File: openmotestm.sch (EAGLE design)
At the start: 46 parts, among them X1 PHB_1MM27_2X05_SNS

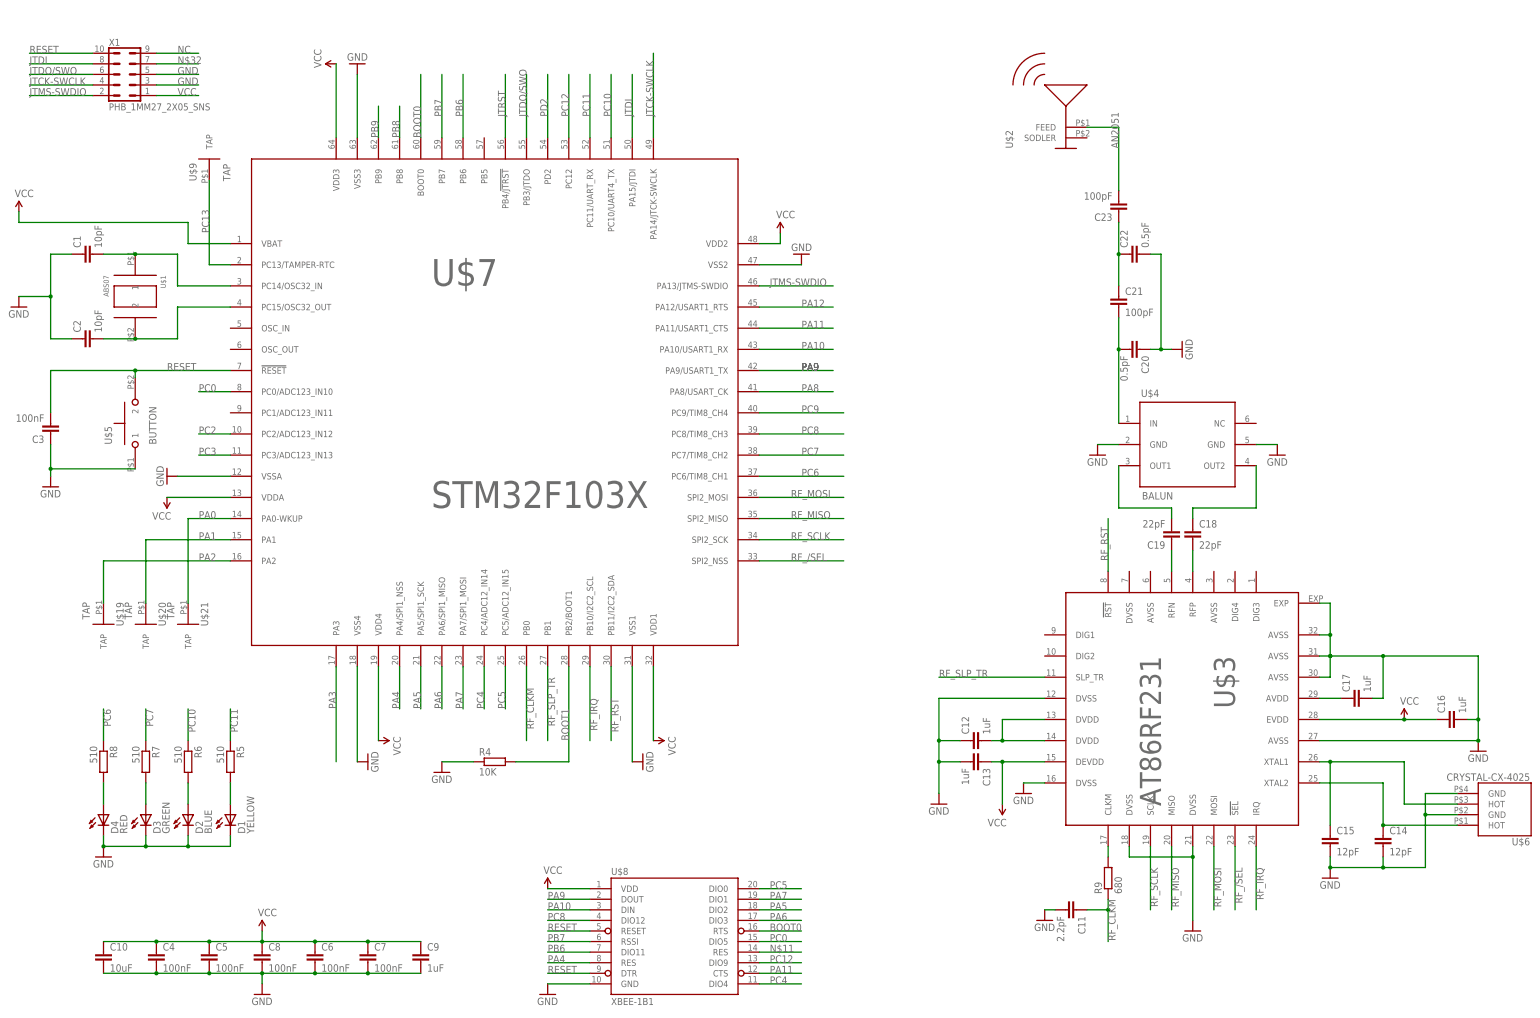
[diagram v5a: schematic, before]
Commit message: Fix the package of chips.
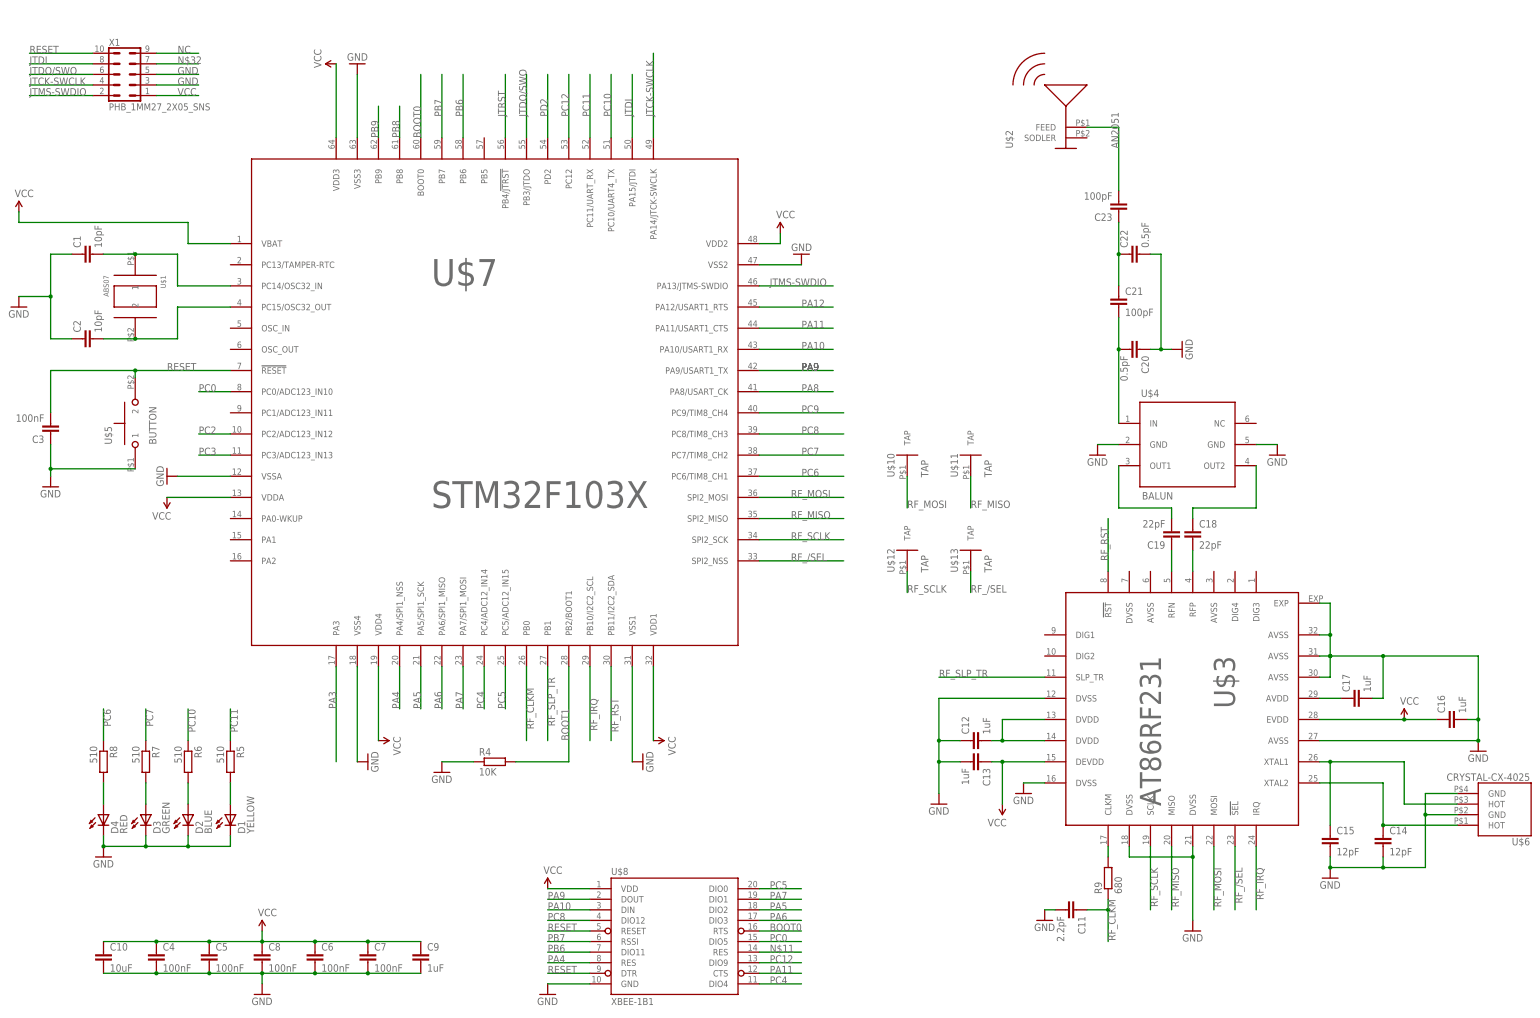
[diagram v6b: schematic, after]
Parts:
- removed U$19, U$20, U$21, U$9: TAP, openmotestm:TAP
- added U$10, U$11, U$12, U$13: TAP, openmotestm:TAP
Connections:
- removed net PA0: U$21.TAP, U$7.PA0-WKUP
- removed net PA1: U$20.TAP, U$7.PA1
- removed net PA2: U$19.TAP, U$7.PA2
- removed net PC13: U$7.PC13/TAMPER-RTC, U$9.TAP
- net RF_/SEL: now also U$13.TAP
- net RF_MISO: now also U$11.TAP
- net RF_MOSI: now also U$10.TAP
- net RF_SCLK: now also U$12.TAP
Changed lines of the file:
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@@
 <layer number="19" name="Unrouted" color="6" fill="1" visible="no" active="no"/>
 <layer number="20" name="Dimension" color="15" fill="1" visible="no" active="no"/>
-<layer number="21" name="tPlace" color="7" fill="1" visible="no" active="no"/>
-<layer number="22" name="bPlace" color="7" fill="1" visible="no" active="no"/>
+<layer number="21" name="tPlace" color="14" fill="1" visible="no" active="no"/>
+<layer number="22" name="bPlace" color="6" fill="1" visible="no" active="no"/>
 <layer number="23" name="tOrigins" color="15" fill="1" visible="no" active="no"/>
 <layer number="24" name="bOrigins" color="15" fill="1" visible="no" active="no"/>
-<layer number="25" name="tNames" color="7" fill="1" visible="no" active="no"/>
+<layer number="25" name="tNames" color="15" fill="1" visible="no" active="no"/>
 <layer number="26" name="bNames" color="7" fill="1" visible="no" active="no"/>
 <layer number="27" name="tValues" color="7" fill="1" visible="no" active="no"/>
@@
 <part name="GND20" library="SparkFun-Aesthetics" deviceset="GND" device=""/>
 <part name="SUPPLY5" library="SparkFun-Aesthetics" deviceset="VCC" device=""/>
-<part name="U$9" library="openmotestm" deviceset="TAP" device=""/>
-<part name="U$19" library="openmotestm" deviceset="TAP" device=""/>
-<part name="U$20" library="openmotestm" deviceset="TAP" device=""/>
-<part name="U$21" library="openmotestm" deviceset="TAP" device=""/>
 <part name="U$6" library="openmotestm" deviceset="CRYSTAL-CX-4025" device=""/>
 <part name="C12" library="rcl" deviceset="C-EU" device="C0603" value="1uF"/>
@@
 <part name="C10" library="rcl" deviceset="C-EU" device="C0603" value="10uF"/>
 <part name="X1" library="_hhn_con_pinhead_box_1mm27" deviceset="PHB_1MM27_2X05_*" device="SNS"/>
+<part name="U$10" library="openmotestm" deviceset="TAP" device=""/>
+<part name="U$11" library="openmotestm" deviceset="TAP" device=""/>
+<part name="U$12" library="openmotestm" deviceset="TAP" device=""/>
+<part name="U$13" library="openmotestm" deviceset="TAP" device=""/>
 </parts>
 <sheets>
@@
 <instance part="GND20" gate="1" x="-134.62" y="25.4" rot="R270"/>
 <instance part="SUPPLY5" gate="G$1" x="-134.62" y="20.32" rot="R180"/>
-<instance part="U$9" gate="G$1" x="-124.46" y="99.06"/>
-<instance part="U$19" gate="G$1" x="-149.86" y="-7.62" rot="R180"/>
-<instance part="U$20" gate="G$1" x="-139.7" y="-7.62" rot="R180"/>
-<instance part="U$21" gate="G$1" x="-129.54" y="-7.62" rot="R180"/>
 <instance part="U$6" gate="G$1" x="185.42" y="-53.34" rot="R180"/>
 <instance part="C12" gate="G$1" x="58.42" y="-38.1" rot="R90"/>
@@
 <instance part="C10" gate="G$1" x="-149.86" y="-88.9"/>
 <instance part="X1" gate="G$1" x="-144.78" y="121.92"/>
+<instance part="U$10" gate="G$1" x="43.18" y="27.94"/>
+<instance part="U$11" gate="G$1" x="58.42" y="27.94"/>
+<instance part="U$12" gate="G$1" x="43.18" y="5.08"/>
+<instance part="U$13" gate="G$1" x="58.42" y="5.08"/>
 </instances>
 <busses>
@@
 <label x="15.24" y="20.32" size="1.778" layer="95"/>
 </segment>
+<segment>
+<pinref part="U$10" gate="G$1" pin="TAP"/>
+<wire x1="43.18" y1="25.4" x2="43.18" y2="17.78" width="0.1524" layer="91"/>
+<label x="43.18" y="17.78" size="1.778" layer="95"/>
+</segment>
 </net>
 <net name="RF_MISO" class="0">
@@
 <label x="15.24" y="15.24" size="1.778" layer="95"/>
 </segment>
+<segment>
+<pinref part="U$11" gate="G$1" pin="TAP"/>
+<wire x1="58.42" y1="25.4" x2="58.42" y2="17.78" width="0.1524" layer="91"/>
+<label x="58.42" y="17.78" size="1.778" layer="95"/>
+</segment>
 </net>
 <net name="RF_SCLK" class="0">
@@
 <label x="15.24" y="10.16" size="1.778" layer="95"/>
 </segment>
+<segment>
+<pinref part="U$12" gate="G$1" pin="TAP"/>
+<wire x1="43.18" y1="2.54" x2="43.18" y2="-2.54" width="0.1524" layer="91"/>
+<label x="43.18" y="-2.54" size="1.778" layer="95"/>
+</segment>
 </net>
 <net name="RF_/SEL" class="0">
@@
 <wire x1="121.92" y1="-63.5" x2="121.92" y2="-78.74" width="0.1524" layer="91"/>
 <label x="121.92" y="-68.58" size="1.778" layer="95" rot="R270"/>
+</segment>
+<segment>
+<pinref part="U$13" gate="G$1" pin="TAP"/>
+<wire x1="58.42" y1="2.54" x2="58.42" y2="-2.54" width="0.1524" layer="91"/>
+<label x="58.42" y="-2.54" size="1.778" layer="95"/>
 </segment>
 </net>
@@
 </segment>
 </net>
-<net name="PC13" class="0">
-<segment>
-<pinref part="U$7" gate="G$1" pin="PC13/TAMPER-RTC"/>
-<wire x1="-119.38" y1="76.2" x2="-124.46" y2="76.2" width="0.1524" layer="91"/>
-<label x="-124.46" y="83.82" size="1.778" layer="95" rot="R90"/>
-<wire x1="-124.46" y1="76.2" x2="-124.46" y2="96.52" width="0.1524" layer="91"/>
-<pinref part="U$9" gate="G$1" pin="TAP"/>
-</segment>
-</net>
 <net name="PC10" class="0">
 <segment>
@@
 </segment>
 </net>
-<net name="PA0" class="0">
-<segment>
-<pinref part="U$7" gate="G$1" pin="PA0-WKUP"/>
-<wire x1="-119.38" y1="15.24" x2="-129.54" y2="15.24" width="0.1524" layer="91"/>
-<pinref part="U$21" gate="G$1" pin="TAP"/>
-<wire x1="-129.54" y1="-5.08" x2="-129.54" y2="15.24" width="0.1524" layer="91"/>
-<label x="-127" y="15.24" size="1.778" layer="95"/>
-</segment>
-</net>
-<net name="PA1" class="0">
-<segment>
-<pinref part="U$7" gate="G$1" pin="PA1"/>
-<wire x1="-119.38" y1="10.16" x2="-139.7" y2="10.16" width="0.1524" layer="91"/>
-<pinref part="U$20" gate="G$1" pin="TAP"/>
-<wire x1="-139.7" y1="-5.08" x2="-139.7" y2="10.16" width="0.1524" layer="91"/>
-<label x="-127" y="10.16" size="1.778" layer="95"/>
-</segment>
-</net>
-<net name="PA2" class="0">
-<segment>
-<pinref part="U$7" gate="G$1" pin="PA2"/>
-<wire x1="-119.38" y1="5.08" x2="-149.86" y2="5.08" width="0.1524" layer="91"/>
-<pinref part="U$19" gate="G$1" pin="TAP"/>
-<wire x1="-149.86" y1="-5.08" x2="-149.86" y2="5.08" width="0.1524" layer="91"/>
-<label x="-127" y="5.08" size="1.778" layer="95"/>
-</segment>
-</net>

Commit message: remove taps.
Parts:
- removed U$10, U$11, U$12, U$13: TAP, openmotestm:TAP
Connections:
- net RF_/SEL: no longer U$13.TAP
- net RF_MISO: no longer U$11.TAP
- net RF_MOSI: no longer U$10.TAP
- net RF_SCLK: no longer U$12.TAP
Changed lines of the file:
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@@
 <part name="C10" library="rcl" deviceset="C-EU" device="C0603" value="10uF"/>
 <part name="X1" library="_hhn_con_pinhead_box_1mm27" deviceset="PHB_1MM27_2X05_*" device="SNS"/>
-<part name="U$10" library="openmotestm" deviceset="TAP" device=""/>
-<part name="U$11" library="openmotestm" deviceset="TAP" device=""/>
-<part name="U$12" library="openmotestm" deviceset="TAP" device=""/>
-<part name="U$13" library="openmotestm" deviceset="TAP" device=""/>
 </parts>
 <sheets>
@@
 <instance part="C10" gate="G$1" x="-149.86" y="-88.9"/>
 <instance part="X1" gate="G$1" x="-144.78" y="121.92"/>
-<instance part="U$10" gate="G$1" x="43.18" y="27.94"/>
-<instance part="U$11" gate="G$1" x="58.42" y="27.94"/>
-<instance part="U$12" gate="G$1" x="43.18" y="5.08"/>
-<instance part="U$13" gate="G$1" x="58.42" y="5.08"/>
 </instances>
 <busses>
@@
 <label x="15.24" y="20.32" size="1.778" layer="95"/>
 </segment>
-<segment>
-<pinref part="U$10" gate="G$1" pin="TAP"/>
-<wire x1="43.18" y1="25.4" x2="43.18" y2="17.78" width="0.1524" layer="91"/>
-<label x="43.18" y="17.78" size="1.778" layer="95"/>
-</segment>
 </net>
 <net name="RF_MISO" class="0">
@@
 <label x="15.24" y="15.24" size="1.778" layer="95"/>
 </segment>
-<segment>
-<pinref part="U$11" gate="G$1" pin="TAP"/>
-<wire x1="58.42" y1="25.4" x2="58.42" y2="17.78" width="0.1524" layer="91"/>
-<label x="58.42" y="17.78" size="1.778" layer="95"/>
-</segment>
 </net>
 <net name="RF_SCLK" class="0">
@@
 <label x="15.24" y="10.16" size="1.778" layer="95"/>
 </segment>
-<segment>
-<pinref part="U$12" gate="G$1" pin="TAP"/>
-<wire x1="43.18" y1="2.54" x2="43.18" y2="-2.54" width="0.1524" layer="91"/>
-<label x="43.18" y="-2.54" size="1.778" layer="95"/>
-</segment>
 </net>
 <net name="RF_/SEL" class="0">
@@
 <label x="121.92" y="-68.58" size="1.778" layer="95" rot="R270"/>
 </segment>
-<segment>
-<pinref part="U$13" gate="G$1" pin="TAP"/>
-<wire x1="58.42" y1="2.54" x2="58.42" y2="-2.54" width="0.1524" layer="91"/>
-<label x="58.42" y="-2.54" size="1.778" layer="95"/>
-</segment>
-</net>
+</net>
